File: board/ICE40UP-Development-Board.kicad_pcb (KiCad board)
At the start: 2 copper layers, 0 parts

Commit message: import board setup
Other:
- copper layers 2 -> 4
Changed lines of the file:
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@@
 (kicad_pcb (version 20211014) (generator pcbnew)
   (general
-    (thickness 1.6)
+    (thickness 1.606)
   )
   (paper "A4")
@@
   (layers
     (0 "F.Cu" signal)
+    (1 "In1.Cu" signal)
+    (2 "In2.Cu" signal)
     (31 "B.Cu" signal)
     (32 "B.Adhes" user "B.Adhesive")
@@
   )
   (setup
+    (stackup
+      (layer "F.SilkS" (type "Top Silk Screen"))
+      (layer "F.Paste" (type "Top Solder Paste"))
+      (layer "F.Mask" (type "Top Solder Mask") (thickness 0.025))
+      (layer "F.Cu" (type "copper") (thickness 0.04))
+      (layer "dielectric 1" (type "core") (thickness 0.138) (material "FR4") (epsilon_r 4.3) (loss_tangent 0.02))
+      (layer "In1.Cu" (type "copper") (thickness 0.035))
+      (layer "dielectric 2" (type "prepreg") (thickness 1.13) (material "FR4") (epsilon_r 4.6) (loss_tangent 0.02))
+      (layer "In2.Cu" (type "copper") (thickness 0.035))
+      (layer "dielectric 3" (type "core") (thickness 0.138) (material "FR4") (epsilon_r 4.3) (loss_tangent 0.02))
+      (layer "B.Cu" (type "copper") (thickness 0.04))
+      (layer "B.Mask" (type "Bottom Solder Mask") (thickness 0.025))
+      (layer "B.Paste" (type "Bottom Solder Paste"))
+      (layer "B.SilkS" (type "Bottom Silk Screen"))
+      (copper_finish "ENIG")
+      (dielectric_constraints no)
+    )
     (pad_to_mask_clearance 0)
     (pcbplotparams

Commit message: start pcb layout; add 3d models
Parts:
- added C1: 100n, Capacitor_SMD:C_0402_1005Metric, F.Cu at (59.8, 93.3)
- added C10: 10n, Capacitor_SMD:C_0402_1005Metric, F.Cu at (65.7, 81.9)
- added C11: 10u, Capacitor_SMD:C_0402_1005Metric, F.Cu at (54.7, 85.7)
- added C12: 1u, Capacitor_SMD:C_0402_1005Metric, F.Cu at (53.7, 85.7)
- added C13: 1u, Capacitor_SMD:C_0402_1005Metric, F.Cu at (53.8, 81.3)
- added C14: 1u, Capacitor_SMD:C_0402_1005Metric, F.Cu at (54.9, 81.3)
- added C15: 10n, Capacitor_SMD:C_0402_1005Metric, F.Cu at (66.7, 93.2)
- added C16: 100n, Capacitor_SMD:C_0402_1005Metric, F.Cu at (64.6, 81.9)
- added C17: 10u, Capacitor_SMD:C_0402_1005Metric, F.Cu at (63.6, 81.9)
- added C18: 100n, Capacitor_SMD:C_0402_1005Metric, F.Cu at (67.9, 85.2)
- added C19: 100n, Capacitor_SMD:C_0402_1005Metric, F.Cu at (77.3, 93.3)
- added C2: 100n, Capacitor_SMD:C_0402_1005Metric, F.Cu at (61.2, 81.9)
- added C20: 1u, Capacitor_SMD:C_0402_1005Metric, F.Cu at (78.4, 93.3)
- added C21: 100n, Capacitor_SMD:C_0402_1005Metric, F.Cu at (79.5, 93.3)
- added C22: 1u, Capacitor_SMD:C_0402_1005Metric, F.Cu at (80.5, 93.3)
- added C3: 100u, Capacitor_SMD:C_0805_2012Metric, F.Cu at (55.1, 94.1)
- added C4: 10u, Capacitor_SMD:C_0402_1005Metric, F.Cu at (52.6, 94.0)
- added C5: 1u, Capacitor_SMD:C_0402_1005Metric, F.Cu at (63.2, 93.3)
- added C6: 100n, Capacitor_SMD:C_0402_1005Metric, F.Cu at (61.2, 93.3)
- added C7: 10n, Capacitor_SMD:C_0402_1005Metric, F.Cu at (62.2, 93.3)
- added C8: 1u, Capacitor_SMD:C_0402_1005Metric, F.Cu at (67.8, 81.9)
- added C9: 100n, Capacitor_SMD:C_0402_1005Metric, F.Cu at (66.8, 81.9)
- added F1: Fuse_Small, Fuse:Fuse_0805_2012Metric, F.Cu at (54.2, 90.9)
- added FB1: FerriteBead_Small, Inductor_SMD:L_0603_1608Metric, F.Cu at (56.4, 91.6)
- added JP1: 1V2EN, Jumper:SolderJumper-2_P1.3mm_Open_RoundedPad1.0x1.5mm, B.Cu at (57.4, 85.3)
- added JP2: 3V3EN, Jumper:SolderJumper-2_P1.3mm_Open_RoundedPad1.0x1.5mm, B.Cu at (57.5, 89.7)
- added R1: 1k5, Resistor_SMD:R_0402_1005Metric, F.Cu at (57.3, 89.4)
- added R10: 10k, Resistor_SMD:R_0402_1005Metric, F.Cu at (77.3, 85.6)
- added R11: 100R, Resistor_SMD:R_0402_1005Metric, F.Cu at (58.1, 83.6)
- added R12: 100R, Resistor_SMD:R_0402_1005Metric, F.Cu at (57.0, 83.6)
- added R13: 100R, Resistor_SMD:R_0402_1005Metric, F.Cu at (56.0, 83.6)
- added R14: 270R, Resistor_SMD:R_0402_1005Metric, F.Cu at (69.3, 82.5)
- added R15: 10k, Resistor_SMD:R_0402_1005Metric, F.Cu at (69.3, 81.5)
- added R16: 10k, Resistor_SMD:R_0402_1005Metric, F.Cu at (80.6, 90.4)
- added R17: 10k, Resistor_SMD:R_0402_1005Metric, F.Cu at (80.6, 88.7)
- added R18: 2k2, Resistor_SMD:R_0402_1005Metric, F.Cu at (49.9, 94.0)
- added R19: 10k, Resistor_SMD:R_0402_1005Metric, F.Cu at (85.2, 82.3)
- added R2: 22R, Resistor_SMD:R_0402_1005Metric, F.Cu at (57.3, 88.4)
- added R3: 5k11, Resistor_SMD:R_0402_1005Metric, F.Cu at (52.5, 81.3)
- added R4: 5k11, Resistor_SMD:R_0402_1005Metric, F.Cu at (51.4, 81.3)
- added R5: 22R, Resistor_SMD:R_0402_1005Metric, F.Cu at (57.3, 87.4)
- added R6: 1Meg, Resistor_SMD:R_0402_1005Metric, F.Cu at (51.3, 94.0)
- added R7: 10k, Resistor_SMD:R_0402_1005Metric, F.Cu at (55.9, 81.3)
- added R8: 100R, Resistor_SMD:R_0402_1005Metric, F.Cu at (62.6, 81.9)
- added R9: 270R, Resistor_SMD:R_0402_1005Metric, F.Cu at (50.0, 81.3)
- added S1: CONF, myLib:SW_SPST_EVQP2, F.Cu at (73.9, 82.4)
- added S2: RST, myLib:SW_SPST_EVQP2, F.Cu at (81.1, 82.4)
- added V1: ICE40UP5K-SG48ITR, Package_DFN_QFN:QFN-48-1EP_7x7mm_P0.5mm_EP5.6x5.6mm, F.Cu at (63.2, 87.6)
- added V2: USBLC6-2P6, Package_TO_SOT_SMD:SOT-666, F.Cu at (54.7, 87.9)
- added V3: TLV7111233DSER, Package_SON:WSON-6_1.5x1.5mm_P0.5mm, F.Cu at (54.4, 83.4)
- added V4: PWR, LED_SMD:LED_0603_1608Metric, F.Cu at (47.8, 81.3)
- added V5: W25Q128JVS, Package_SO:SOIC-8_5.23x5.23mm_P1.27mm, F.Cu at (73.8, 89.7)
- added V6: LED_RGBA, myLib:CREE_UHD111A, F.Cu at (59.7, 81.9)
- added V7: CONF, LED_SMD:LED_0603_1608Metric, F.Cu at (69.3, 84.7)
- added V8: APS6404L, Package_SON:SON-8-1EP_3x2mm_P0.5mm_EP1.4x1.6mm, F.Cu at (78.8, 89.5)
- added V9: CDONE, LED_SMD:LED_0603_1608Metric, F.Cu at (47.8, 94.0)
- added X1: USB4105-GF-A, Connector_USB:USB_C_Receptacle_G-Switch_GT-USB-7010ASV, F.Cu at (48.3, 87.6)
- added X2: Conn_01x16, Connector_PinHeader_2.54mm:PinHeader_1x16_P2.54mm_Vertical, B.Cu at (47.1, 78.7)
- added X3: Conn_01x16, Connector_PinHeader_2.54mm:PinHeader_1x16_P2.54mm_Vertical, B.Cu at (47.1, 96.5)
- added X4: Tag-Connect, Connector:Tag-Connect_TC2050-IDC-NL_2x05_P1.27mm_Vertical, F.Cu at (83.9, 89.9)
- added Y1: 48MHz, Oscillator:Oscillator_SMD_Abracon_ASE-4Pin_3.2x2.5mm, F.Cu at (69.1, 92.1)
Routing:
- net GND: track 0.00 -> 36.3 mm, vias 0 -> 30
- net +3V3: track 0.00 -> 31.8 mm, vias 0 -> 15
- net SPI_SO: track 0.00 -> 29.4 mm, vias 0 -> 2
- net FLASH_~{SS}: track 0.00 -> 29.3 mm, vias 0 -> 2
- net SPI_~{HOLD}: track 0.00 -> 28.9 mm, vias 0 -> 4
- net RAM_~{SS}: track 0.00 -> 28.4 mm, vias 0 -> 2
- net SPI_SCK: track 0.00 -> 28.0 mm, vias 0 -> 2
- net SPI_~{WP}: track 0.00 -> 23.6 mm, vias 0 -> 2
- net SPI_SI: track 0.00 -> 21.2 mm, vias 0 -> 3
- net VBUS: track 0.00 -> 17.5 mm, vias 0 -> 2
- net Net-(R4-Pad1): track 0.00 -> 10.7 mm, vias 0 -> 2
- net Net-(F1-Pad1): track 0.00 -> 9.86 mm
- net +1V2: track 0.00 -> 9.48 mm, vias 0 -> 5
- net ~{CONF}_I: track 0.00 -> 8.52 mm, vias 0 -> 1
- net ~{RST}: track 0.00 -> 8.00 mm, vias 0 -> 1
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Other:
- board outline added: 41 x 20.3 mm

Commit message: initial pcb layout
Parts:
- removed the R6 at (51.3, 94.0)
- X2, X3: value Conn_01x16 -> Conn_01x17; footprint Connector_PinHeader_2.54mm:PinHeader_1x16_P2.54mm_Vertical -> Connector_PinHeader_2.54mm:PinHeader_1x17_P2.54mm_Vertical
- X4: footprint Connector:Tag-Connect_TC2050-IDC-NL_2x05_P1.27mm_Vertical -> Connector:Tag-Connect_TC2050-IDC-FP_2x05_P1.27mm_Vertical
- moved R5 6.56 mm to (57.9, 81.7)
- moved C5 5.43 mm to (56.5, 90.3), turned to 0 degrees
- moved JP1 5.23 mm to (52.7, 87.6), turned to 180 degrees
- moved C3 3.22 mm to (57.9, 92.6), turned to -90 degrees
- moved R4 3.12 mm to (55.6, 81.7)
- moved R16 2.93 mm to (47.1, 81.5), turned to 180 degrees
- moved R17 2.81 mm to (47.1, 93.7), turned to 180 degrees
- moved R3 2.72 mm to (79.0, 86.5), turned to -90 degrees
- moved R1 2.57 mm to (78.5, 91.8), turned to 180 degrees
- moved JP2 2.32 mm to (56.5, 87.6)
- moved C8 2.22 mm to (80.0, 91.2)
- moved R12 1.97 mm to (83.3, 82.8)
- moved V5 1.92 mm to (49.7, 81.5), turned to 180 degrees
- moved V9 1.90 mm to (49.6, 93.7), turned to 180 degrees
- moved S2 1.50 mm to (79.6, 82.5)
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- renumbered C16 to C1, C22 to C10, C13 to C11, C14 to C12, C5 to C13, C6 to C14, C7 to C15, C15 to C16, C8 to C17, C1 to C18, C9 to C19, C17 to C2, C10 to C20, C18 to C21, C2 to C22, C11 to C4, C4 to C5, C12 to C6, C19 to C7, C21 to C8, C20 to C9, R16 to R1, R5 to R10, R15 to R11, R19 to R12, R11 to R13, R12 to R14, R13 to R15, R9 to R16, R18 to R17, R14 to R18, R10 to R2, R17 to R3, R3 to R4, R4 to R5, R8 to R6, R1 to R8, R2 to R9, V5 to V1, V8 to V2, V2 to V4, V4 to V5, V1 to V6, V6 to V7, V7 to V8
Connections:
- C16 pad 1: GND -> +3V3
- C16 pad 2: +3V3 -> GND
- V6 pad 18: SPI_~{HOLD} -> SPI_~{WP}
- V6 pad 19: SPI_~{WP} -> SPI_~{HOLD}
- V6 pad 20: RAM_~{SS} -> IOB_25b
- V6 pad 21: IOB_23b -> RAM_~{SS}
- X1 pad S1: Net-(R6-Pad1) -> GND
- X2 pad 10: IOT_44b -> IOT_39a
- X2 pad 11: IOT_45a -> IOT_38b
- X2 pad 12: IOB_8a -> IOT_37b
- X2 pad 13: IOB_0a -> IOT_36b
- X2 pad 14: IOB_2a -> IOB_25b
- X2 pad 15: RAM_~{SS} -> SPI_~{WP}
- X2 pad 16: GND -> SPI_SI
- X2 pad 3: IOT_36b -> IOT_48b
- X2 pad 4: IOT_37b -> IOT_46b
- X2 pad 5: IOT_38b -> IOT_45a
- X2 pad 6: IOT_39a -> IOT_44b
- X2 pad 7: IOT_41a -> IOT_43a
- X2 pad 9: IOT_43a -> IOT_41a
- X3 pad 10: IOT_46b -> IOB_18a
- X3 pad 11: IOB_23b -> IOB_20a
- X3 pad 13: SPI_SO -> RAM_~{SS}
- X3 pad 14: SPI_SI -> SPI_SO
- X3 pad 16: FLASH_~{SS} -> SPI_~{HOLD}
- X3 pad 2: IOB_3b -> IOB_0a
- X3 pad 3: IOB_4a -> IOB_2a
- X3 pad 4: IOT_48b -> IOB_3b
- X3 pad 5: IOB_6a -> IOB_4a
- X3 pad 6: IOB_13b -> IOB_6a
- X3 pad 7: IOB_16a -> IOB_8a
- X3 pad 8: IOB_18a -> IOB_13b
- X3 pad 9: IOB_20a -> IOB_16a
- X4 pad 1: unconnected-(X4-Pad1) -> +3V3
- X4 pad 10: FLASH_~{SS} -> CDONE
- X4 pad 2: GND -> FLASH_~{SS}
- X4 pad 3: unconnected-(X4-Pad3) -> GND
- X4 pad 4: unconnected-(X4-Pad4) -> SPI_SCK
- X4 pad 6: SPI_~{HOLD} -> SPI_SI
- X4 pad 7: SPI_SI -> RAM_~{SS}
- X4 pad 9: SPI_SCK -> SPI_~{HOLD}
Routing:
- net CDONE: track 3.48 -> 44.3 mm, vias 2 -> 5
- net IOB_25b: track 0.00 -> 20.2 mm
- net ~{RST}: track 8.00 -> 27.8 mm, vias 1 -> 3
- net +1V2: track 9.48 -> 26.0 mm, vias 5 -> 4
- net ~{CONF}_I: track 8.52 -> 24.4 mm, vias 1 -> 2
- net IOT_36b: track 0.56 -> 16.2 mm
- net IOB_24a: track 0.75 -> 13.0 mm, vias 1 -> 0
- net SPI_SI: track 21.2 -> 33.4 mm, vias 3 -> 1
- net IOB_0a: track 2.93 -> 14.8 mm
- net CONF_O: track 1.57 -> 13.1 mm, vias 1 -> 2
- net IOB_3b: track 1.38 -> 12.3 mm, vias 1 -> 2
- net IOT_48b: track 0.67 -> 11.5 mm
- net IOT_37b: track 1.89 -> 12.6 mm
- net IOT_38b: track 1.10 -> 11.6 mm
- net SPI_~{WP}: track 23.6 -> 33.4 mm, vias 2 -> 0
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- added copper zone on B.Cu, net (none)
- added copper zone on F.Cu, net (none)
- added copper zone on In2.Cu, net +1V2
- added copper zone on In2.Cu, net +3V3
- added copper zone on In1.Cu, net GND
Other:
- board size 41 x 20.3 mm -> 43.3 x 20.3 mm
- board text added: "1V2"
- board text added: "3V3"
- board text added: "5V"
- board text added: "B0"
- board text added: "B13"
- board text added: "B16"
- board text added: "B18"
- board text added: "B2"
- board text added: "B20"
- board text added: "B24"
- board text added: "B25"
- board text added: "B29"
- board text added: "B3"
- board text added: "B31"
- board text added: "B4"
- board text added: "B6"
- board text added: "B8"
- board text added: "BTN0"
- board text added: "CDONE"
- board text added: "G"
- board text added: "LED0"
- board text added: "PWR"
- board text added: "RST"
- board text added: "SCK"
- board text added: "SDI"
- board text added: "SDO"
- board text added: "T36"
- board text added: "T37"
- board text added: "T38"
- board text added: "T39"
- board text added: "T41"
- board text added: "T42"
- board text added: "T43"
- board text added: "T44"
- board text added: "T45"
- board text added: "T46"
- board text added: "T48"
- board text added: "csF"
- board text added: "csR"

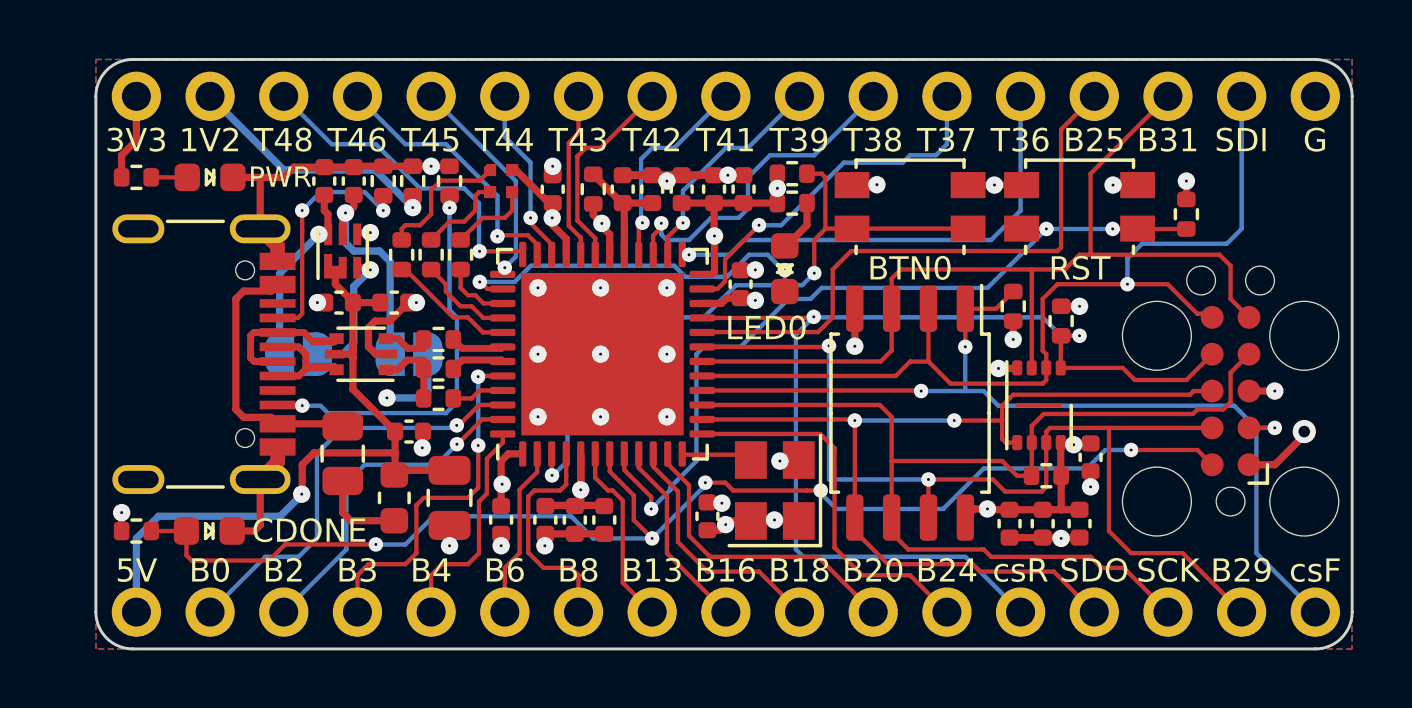
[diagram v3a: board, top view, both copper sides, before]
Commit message: decrease pcb size; remove SPI-SS signals from breakout pins
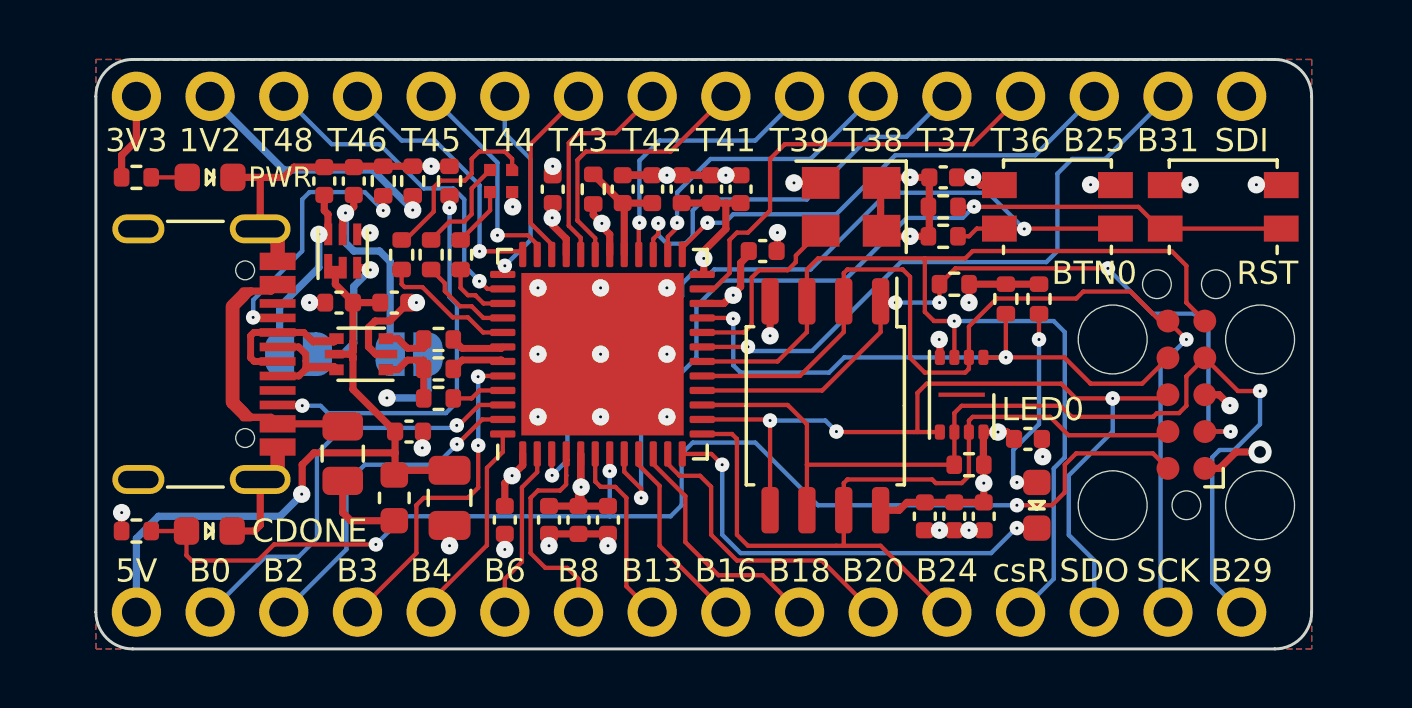
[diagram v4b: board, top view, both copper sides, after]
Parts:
- X2, X3: value Conn_01x17 -> Conn_01x16; footprint Connector_PinHeader_2.54mm:PinHeader_1x17_P2.54mm_Vertical -> Connector_PinHeader_2.54mm:PinHeader_1x16_P2.54mm_Vertical
- moved C15 14.2 mm to (74.9, 81.5), turned to 0 degrees
- moved V8 11.9 mm to (78.2, 92.8)
- moved Y1 10.1 mm to (71.8, 82.5), turned to 180 degrees
- moved R18 9.13 mm to (78.2, 85.7), turned to 90 degrees
- moved R12 8.39 mm to (74.9, 82.5), turned to 0 degrees
- moved R11 5.64 mm to (74.9, 83.6)
- moved S1 5.08 mm to (78.9, 82.5)
- moved S2 4.95 mm to (84.6, 82.5)
- moved C10 3.31 mm to (76.3, 93.2)
- moved C9 3.06 mm to (75.3, 93.2)
- moved V1 2.93 mm to (70.9, 89.4)
- moved C7 2.93 mm to (74.3, 93.2)
- moved R1 2.69 mm to (75.8, 91.4)
- moved V2 2.69 mm to (75.6, 89.0)
- moved C8 2.25 mm to (77.9, 90.6), turned to 180 degrees
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- renumbered C16 to C15, C15 to C16, C22 to C21, C21 to C22, R6 to R4, R4 to R5, R5 to R6
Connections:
- V6 pad 12: CLK -> CONF_O
- V6 pad 13: IOB_24a -> SPI_~{HOLD}
- V6 pad 19: SPI_~{HOLD} -> IOB_29b
- V6 pad 20: IOB_25b -> CLK
- V6 pad 38: CONF_O -> IOT_50b
- X2 pad 10: IOT_39a -> IOT_41a
- X2 pad 11: IOT_38b -> IOT_39a
- X2 pad 12: IOT_37b -> IOT_38b
- X2 pad 13: IOT_36b -> IOT_37b
- X2 pad 14: IOB_25b -> IOT_36b
- X2 pad 15: SPI_~{WP} -> IOB_29b
- X2 pad 16: SPI_SI -> GND
- X2 pad 3: IOT_48b -> IOT_50b
- X2 pad 4: IOT_46b -> IOT_48b
- X2 pad 5: IOT_45a -> IOT_46b
- X2 pad 6: IOT_44b -> IOT_45a
- X2 pad 7: IOT_43a -> IOT_44b
- X2 pad 8: IOT_42b -> IOT_43a
- X2 pad 9: IOT_41a -> IOT_42b
- X3 pad 12: IOB_24a -> SPI_~{HOLD}
- X3 pad 13: RAM_~{SS} -> SPI_~{WP}
- X3 pad 15: SPI_SCK -> SPI_SI
- X3 pad 16: SPI_~{HOLD} -> SPI_SCK
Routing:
- net IOB_29b: track 0.00 -> 21.3 mm, vias 0 -> 1
- net IOB_25b: track 20.2 -> 0.00 mm
- net RAM_~{SS}: track 37.7 -> 21.0 mm
- net IOB_24a: track 13.0 -> 0.00 mm
- net IOT_50b: track 0.00 -> 11.7 mm, vias 0 -> 1
- net SPI_~{WP}: track 33.4 -> 40.4 mm, vias 0 -> 1
- net FLASH_~{SS}: track 33.1 -> 26.2 mm, vias 3 -> 4
- net SPI_~{HOLD}: track 35.1 -> 28.7 mm, vias 2 -> 0
- net ~{CONF}_I: track 24.4 -> 30.1 mm
- net Net-(V8-A): track 1.82 -> 6.92 mm, vias 0 -> 2
- net Net-(F1-Pad1): track 9.38 -> 13.8 mm
- net CLK: track 2.38 -> 6.64 mm
- net ~{RST}: track 27.8 -> 31.6 mm, vias 3 -> 2
- net IOT_37b: track 12.6 -> 15.4 mm, vias 1 -> 0
- net IOT_38b: track 11.6 -> 14.2 mm
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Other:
- board size 43.3 x 20.3 mm -> 41.9 x 20.3 mm
- board text removed: "G"
- board text removed: "csF"

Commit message: increase size of RAM pads
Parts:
- moved V8 6.73 mm to (78.1, 86.1)
- moved C8 2.62 mm to (77.3, 93.1), turned to 90 degrees
- moved R1 2.05 mm to (77.5, 90.2), turned to 90 degrees
- moved R18 1.40 mm to (76.8, 85.6)
- moved R3 1.40 mm to (75.7, 85.6)
- moved R2 0.85 mm to (74.5, 85.6), turned to -90 degrees
- moved X2 0.51 mm to (47.6, 78.7)
- moved X3 0.51 mm to (47.6, 96.5)
- moved V2 0.44 mm to (75.6, 89.5)
- moved C10 0.10 mm to (76.3, 93.1)
- moved C7 0.10 mm to (74.3, 93.1)
- moved C9 0.10 mm to (75.3, 93.1)
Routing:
- net Net-(V8-A): track 6.92 -> 1.61 mm, vias 2 -> 0
- net CONF_O: track 15.7 -> 20.3 mm
- net SPI_SI: track 35.1 -> 37.2 mm
- net SPI_~{WP}: track 40.4 -> 38.6 mm
- net CDONE: track 43.2 -> 42.2 mm
- net ~{RST}: track 31.6 -> 30.6 mm
- net SPI_~{HOLD}: track 28.7 -> 28.1 mm
- net SPI_SO: track 30.2 -> 29.5 mm
- net IOT_39a: track 10.4 -> 10.9 mm
- net IOT_37b: track 15.4 -> 15.9 mm
- net IOB_0a: track 14.8 -> 14.3 mm
- net IOT_38b: track 14.2 -> 14.8 mm
- net IOT_42b: track 9.54 -> 10.0 mm
- net IOT_50b: track 11.7 -> 11.1 mm
- net IOT_43a: track 7.56 -> 8.07 mm
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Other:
- board text added: "B32"
- board text added: "B33"
- board text added: "B34"
- board text added: "GND"
- board text added: "T50"
- board text removed: "B25"
- board text removed: "SCK"
- board text removed: "SDI"
- board text removed: "SDO"
- board text removed: "csR"
